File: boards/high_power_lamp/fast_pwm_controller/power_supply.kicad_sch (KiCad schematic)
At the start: 13 parts

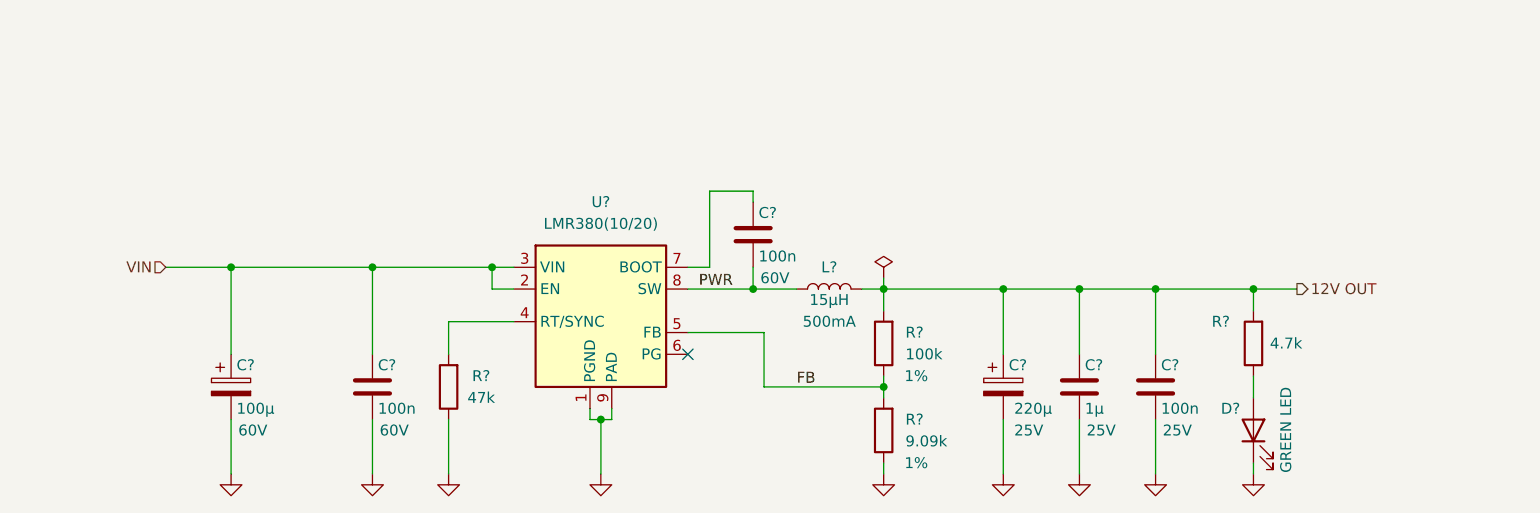
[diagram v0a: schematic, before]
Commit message: buck converter can now be switched off via jumper
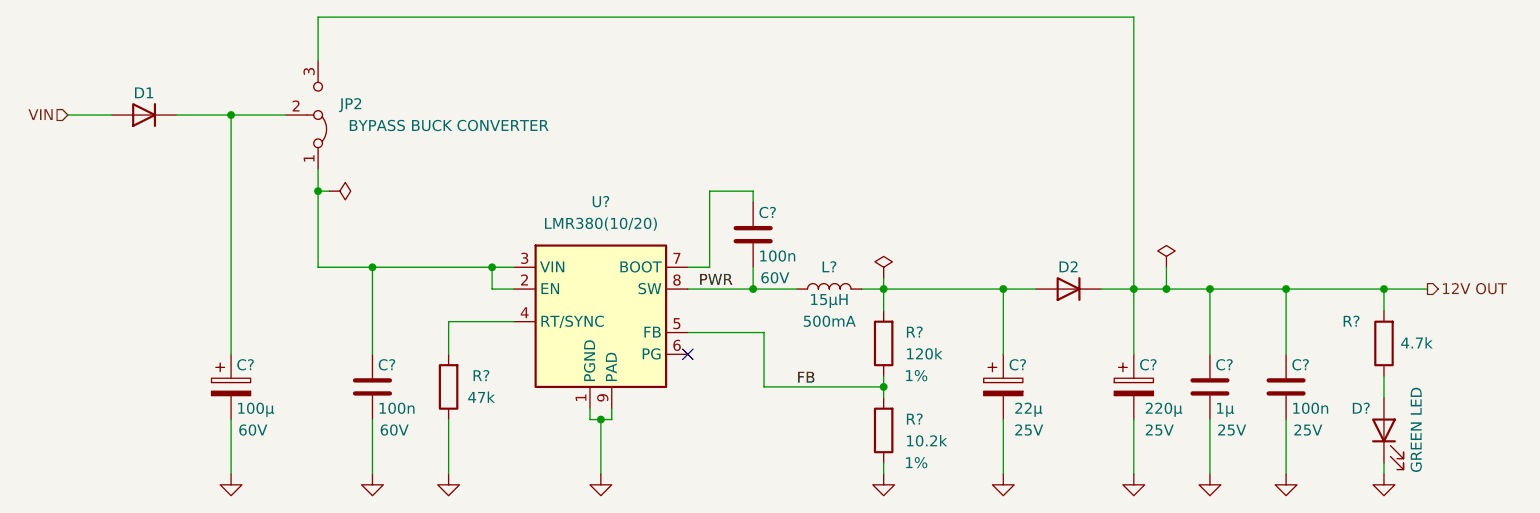
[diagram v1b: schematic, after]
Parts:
- added C?: 22μ, Capacitor_THT:CP_Radial_D5.0mm_P2.00mm, symbol Device:C_Polarized
- added D1, D2: 1N4148, Diode_SMD:D_SOD-123, symbol Device:D
- added JP2: Jumper_3, Connector_PinHeader_2.54mm:PinHeader_1x03_P2.54mm_Vertical, symbol Jumper:Jumper_3_Bridged12
- R?: value 9.09k -> 10.2k
- R?: value 100k -> 120k
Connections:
- net 12V OUT: now also D2.1 (K), JP2.3 (B); no longer L?.2, R?.2
- net GND: now also C?.2
- net VIN: now also D1.2 (A); no longer C?.1, C?.1, U?.2 (EN), U?.3 (VIN)
- new net: C?.1, D1.1 (K), JP2.2 (C)
- new net: C?.1, JP2.1 (A), U?.2 (EN), U?.3 (VIN)
- new net: C?.1, D2.2 (A), L?.2, R?.2
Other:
- moved on the sheet: C?, D?, R?
